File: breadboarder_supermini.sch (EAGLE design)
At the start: 22 parts, among them IC1 AVR-MEGA8-PPTH, Q1 MOSFET-NCHANNEL2N7000

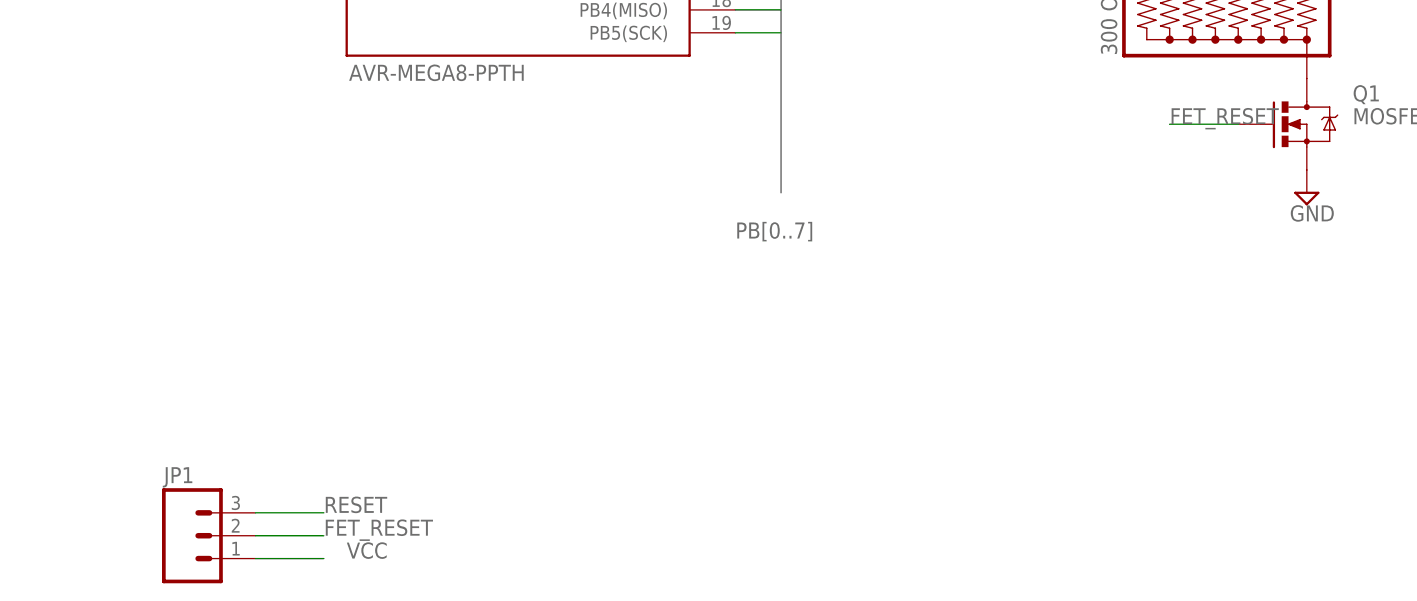
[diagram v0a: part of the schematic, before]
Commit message: bug with led fet fixed
now can pull to reset line or ground(!), disabling LEDs
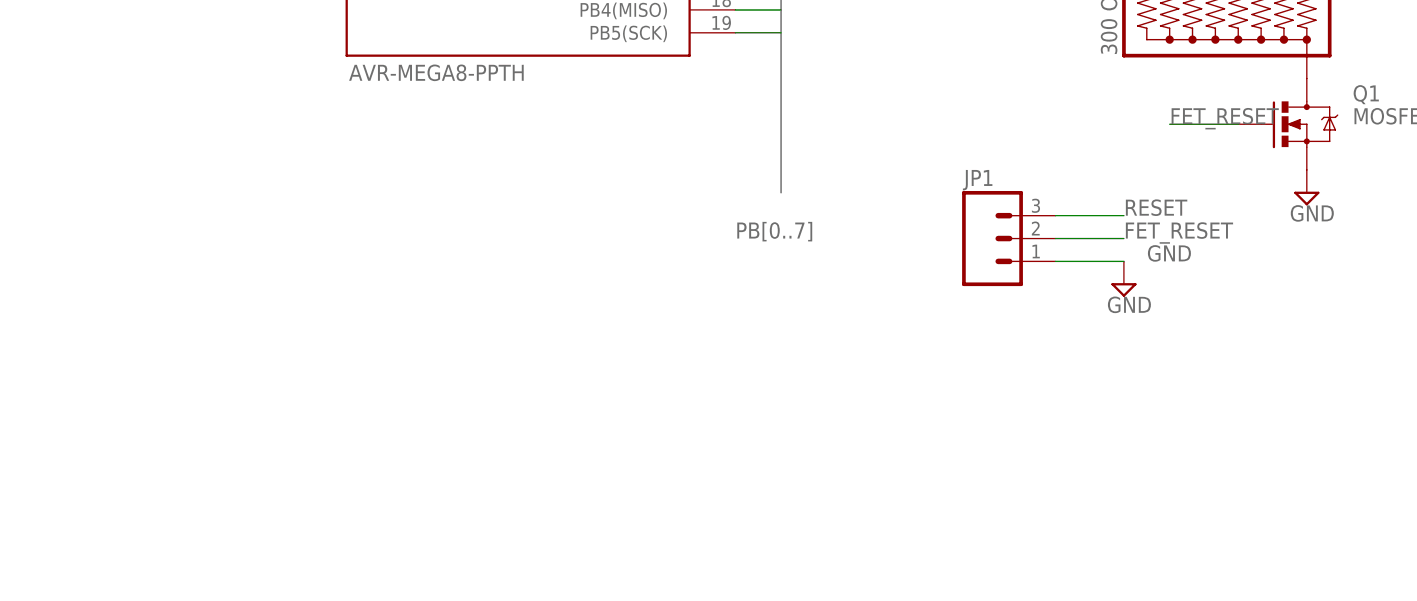
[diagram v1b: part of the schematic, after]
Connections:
- net GND: now also JP1.1
- net VCC: no longer JP1.1
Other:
- moved on the sheet: JP1
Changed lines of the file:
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@@
 <part name="SUPPLY4" library="supply2" deviceset="GND" device=""/>
 <part name="SUPPLY5" library="supply2" deviceset="GND" device=""/>
+<part name="SUPPLY6" library="supply2" deviceset="GND" device=""/>
 </parts>
 <sheets>
@@
 <instance part="C2" gate="G$1" x="0" y="30.48"/>
 <instance part="SUPPLY7" gate="GND" x="0" y="20.32"/>
-<instance part="JP1" gate="G$1" x="25.4" y="-48.26"/>
+<instance part="JP1" gate="G$1" x="114.3" y="-15.24"/>
 <instance part="RESET" gate="S" x="-38.1" y="7.62"/>
 <instance part="BUTTON" gate="S" x="-38.1" y="25.4"/>
 <instance part="SUPPLY4" gate="GND" x="-33.02" y="2.54"/>
 <instance part="SUPPLY5" gate="GND" x="-33.02" y="20.32"/>
+<instance part="SUPPLY6" gate="GND" x="129.54" y="-20.32"/>
 </instances>
 <busses>
@@
 <junction x="-33.02" y="22.86"/>
 </segment>
+<segment>
+<pinref part="JP1" gate="G$1" pin="1"/>
+<wire x1="121.92" y1="-17.78" x2="129.54" y2="-17.78" width="0.1524" layer="91"/>
+<label x="132.08" y="-17.78" size="1.778" layer="95"/>
+<pinref part="SUPPLY6" gate="GND" pin="GND"/>
+</segment>
 </net>
 <net name="VCC" class="0">
@@
 <label x="71.12" y="111.76" size="1.778" layer="95"/>
 </segment>
-<segment>
-<pinref part="JP1" gate="G$1" pin="1"/>
-<wire x1="33.02" y1="-50.8" x2="40.64" y2="-50.8" width="0.1524" layer="91"/>
-<label x="43.18" y="-50.8" size="1.778" layer="95"/>
-</segment>
 </net>
 <net name="AREF" class="0">
@@
 <segment>
 <pinref part="JP1" gate="G$1" pin="3"/>
-<wire x1="33.02" y1="-45.72" x2="40.64" y2="-45.72" width="0.1524" layer="91"/>
-<label x="40.64" y="-45.72" size="1.778" layer="95"/>
+<wire x1="121.92" y1="-12.7" x2="129.54" y2="-12.7" width="0.1524" layer="91"/>
+<label x="129.54" y="-12.7" size="1.778" layer="95"/>
 </segment>
 <segment>
@@
 <segment>
 <pinref part="JP1" gate="G$1" pin="2"/>
-<wire x1="33.02" y1="-48.26" x2="40.64" y2="-48.26" width="0.1524" layer="91"/>
-<label x="40.64" y="-48.26" size="1.778" layer="95"/>
-</segment>
-</net>
+<wire x1="121.92" y1="-15.24" x2="129.54" y2="-15.24" width="0.1524" layer="91"/>
+<label x="129.54" y="-15.24" size="1.778" layer="95"/>
+</segment>
+</net>
